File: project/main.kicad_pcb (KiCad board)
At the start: 6 copper layers, 160 x 257 mm, 207 parts

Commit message: adding comunication cable numbers
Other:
- board text added: "101"
- board text added: "102"
- board text added: "103"
- board text added: "106"
- board text added: "107"
- board text added: "108"
- board text added: "111"
- board text added: "112"
- board text added: "117"
- board text added: "118"
- board text added: "119"
- board text added: "120"
- board text added: "121"
- board text added: "122"
- board text added: "123"
- board text added: "217"
- board text added: "218"
- board text added: "219"
- board text added: "220"
- board text added: "221"
- board text added: "222"
- board text added: "223"
- board text added: "224"
- board text added: "317"
- board text added: "318"
- board text added: "3xx"
- board text added: "EL music 18m"
- board text added: "cam-dirty1 21m"
- board text added: "cam-dirty2 34m"
- board text added: "cam-laser 34m"
- board text added: "cam-storage1 16m"
- board text removed: "000"
- board text removed: "EL audio 18m"
- board text removed: "cam-purvinos1 21m"
- board text removed: "cam-purvinos2 34m"
- board text removed: "cam-sandelis1 16m"
- board text removed: "cam-staklide1 34m"
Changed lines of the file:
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@@
       (layer "F.SilkS" (type "Top Silk Screen") (color "Black"))
       (layer "F.Paste" (type "Top Solder Paste"))
-      (layer "F.Mask" (type "Top Solder Mask") (color "White") (thickness 0.01))
+      (layer "F.Mask" (type "Top Solder Mask") (thickness 0.01))
       (layer "F.Cu" (type "copper") (thickness 0.035))
-      (layer "dielectric 1" (type "core") (thickness 0.274) (material "FR4") (epsilon_r 4.5) (loss_tangent 0.02))
+      (layer "dielectric 1" (type "prepreg") (thickness 0.274) (material "FR4") (epsilon_r 4.5) (loss_tangent 0.02))
       (layer "In1.Cu" (type "copper") (thickness 0.035))
       (layer "dielectric 2" (type "prepreg") (thickness 0.274) (material "FR4") (epsilon_r 4.5) (loss_tangent 0.02))
@@
     (effects (font (size 2 2) (thickness 0.3)) (justify left))
   )
-  (gr_text "000" (at 170.28 50.32) (layer "User.5")
+  (gr_text "123" (at 170.28 50.32) (layer "User.5")
     (effects (font (size 1 1) (thickness 0.15)))
   )
@@
     (effects (font (size 1 1) (thickness 0.15)) (justify left))
   )
-  (gr_text "cam-sandelis1 16m" (at 42.28 145.32) (layer "User.5")
+  (gr_text "cam-storage1 16m" (at 42.28 145.32) (layer "User.5")
     (effects (font (size 2 2) (thickness 0.3)) (justify left))
   )
@@
     (effects (font (size 2 2) (thickness 0.3)) (justify left))
   )
-  (gr_text "000" (at 177.28 184.32) (layer "User.5")
+  (gr_text "106" (at 177.28 184.32) (layer "User.5")
     (effects (font (size 1 1) (thickness 0.15)))
   )
@@
     (effects (font (size 2 2) (thickness 0.3)) (justify left))
   )
-  (gr_text "000" (at 159.28 111.32) (layer "User.5")
+  (gr_text "102" (at 159.28 111.32) (layer "User.5")
     (effects (font (size 1 1) (thickness 0.15)))
   )
-  (gr_text "000" (at 129.28 207.32) (layer "User.5")
+  (gr_text "219" (at 129.28 207.32) (layer "User.5")
     (effects (font (size 1 1) (thickness 0.15)))
   )
@@
     (effects (font (size 1 1) (thickness 0.15)) (justify left))
   )
-  (gr_text "cam-staklide1\n34m" (at 174.28 47.32) (layer "User.5")
+  (gr_text "cam-laser\n34m" (at 174.28 47.32) (layer "User.5")
     (effects (font (size 2 2) (thickness 0.3)) (justify left))
   )
-  (gr_text "000" (at 196.28 65.32) (layer "User.5")
+  (gr_text "122" (at 196.28 65.32) (layer "User.5")
     (effects (font (size 1 1) (thickness 0.15)))
   )
@@
     (effects (font (size 2 2) (thickness 0.3)) (justify left))
   )
-  (gr_text "cam-purvinos1 21m" (at 43.28 111.32) (layer "User.5")
+  (gr_text "cam-dirty1 21m" (at 48.78 111.32) (layer "User.5")
     (effects (font (size 2 2) (thickness 0.3)) (justify left))
   )
@@
     (effects (font (size 1 1) (thickness 0.15)) (justify left))
   )
-  (gr_text "000" (at 115.28 86.32) (layer "User.5")
+  (gr_text "107" (at 115.28 86.32) (layer "User.5")
     (effects (font (size 1 1) (thickness 0.15)))
   )
-  (gr_text "000" (at 196.28 228.32) (layer "User.5")
+  (gr_text "118" (at 196.28 228.32) (layer "User.5")
     (effects (font (size 1 1) (thickness 0.15)))
   )
@@
     (effects (font (size 1 1) (thickness 0.15)) (justify left))
   )
-  (gr_text "000" (at 159.28 63.32) (layer "User.5")
+  (gr_text "111" (at 159.28 63.32) (layer "User.5")
     (effects (font (size 1 1) (thickness 0.15)))
   )
-  (gr_text "000" (at 174.28 231.32) (layer "User.5")
+  (gr_text "318" (at 174.28 231.32) (layer "User.5")
     (effects (font (size 1 1) (thickness 0.15)))
   )
@@
     (effects (font (size 1 1) (thickness 0.15)) (justify left))
   )
-  (gr_text "000" (at 155.28 268.32) (layer "User.5")
+  (gr_text "119" (at 155.28 268.32) (layer "User.5")
     (effects (font (size 1 1) (thickness 0.15)))
   )
@@
     (effects (font (size 2 2) (thickness 0.3)) (justify left))
   )
-  (gr_text "cam-el1 11m" (at 209.28 228.32) (layer "User.5")
+  (gr_text "cam-el2 11m" (at 209.28 228.32) (layer "User.5")
     (effects (font (size 2 2) (thickness 0.3)) (justify left))
   )
-  (gr_text "000" (at 86.28 111.32) (layer "User.5")
+  (gr_text "121" (at 86.28 111.32) (layer "User.5")
     (effects (font (size 1 1) (thickness 0.15)))
   )
@@
     (effects (font (size 2 2) (thickness 0.3)) (justify left))
   )
-  (gr_text "000" (at 128.28 184.32) (layer "User.5")
+  (gr_text "117" (at 128.28 184.32) (layer "User.5")
     (effects (font (size 1 1) (thickness 0.15)))
   )
@@
     (effects (font (size 1 1) (thickness 0.15)) (justify left))
   )
-  (gr_text "000" (at 115.28 42.32) (layer "User.5")
+  (gr_text "101" (at 115.28 42.32) (layer "User.5")
     (effects (font (size 1 1) (thickness 0.15)))
   )
@@
     (effects (font (size 1 1) (thickness 0.15)) (justify left))
   )
-  (gr_text "cam-purvinos2 34m" (at 208.28 65.32) (layer "User.5")
+  (gr_text "cam-dirty2 34m" (at 208.28 65.32) (layer "User.5")
     (effects (font (size 2 2) (thickness 0.3)) (justify left))
   )
@@
     (effects (font (size 1 1) (thickness 0.15)) (justify left))
   )
-  (gr_text "000" (at 133.28 231.32) (layer "User.5")
+  (gr_text "217" (at 133.28 231.32) (layer "User.5")
     (effects (font (size 1 1) (thickness 0.15)))
   )
@@
     (effects (font (size 1 1) (thickness 0.15)) (justify left))
   )
-  (gr_text "000" (at 202.28 184.32) (layer "User.5")
+  (gr_text "221" (at 202.28 184.32) (layer "User.5")
     (effects (font (size 1 1) (thickness 0.15)))
   )
@@
     (effects (font (size 2 2) (thickness 0.3)) (justify left))
   )
-  (gr_text "EL\naudio\n18m" (at 129.28 218.32) (layer "User.5")
+  (gr_text "EL\nmusic\n18m" (at 129.28 218.32) (layer "User.5")
     (effects (font (size 2 2) (thickness 0.3)) (justify left))
   )
@@
     (effects (font (size 2 2) (thickness 0.3)) (justify left))
   )
-  (gr_text "000" (at 170.28 39.32) (layer "User.5")
+  (gr_text "224" (at 170.28 39.32) (layer "User.5")
     (effects (font (size 1 1) (thickness 0.15)))
   )
@@
     (effects (font (size 2 2) (thickness 0.3)) (justify left))
   )
-  (gr_text "000" (at 133.28 184.32) (layer "User.5")
+  (gr_text "112" (at 133.28 184.32) (layer "User.5")
     (effects (font (size 1 1) (thickness 0.15)))
   )
-  (gr_text "000" (at 99.28 214.82) (layer "User.5")
+  (gr_text "218" (at 99.28 214.82) (layer "User.5")
     (effects (font (size 1 1) (thickness 0.15)))
   )
@@
     (effects (font (size 1 1) (thickness 0.15)) (justify left))
   )
-  (gr_text "cam-el2\n11m" (at 112.28 189.32) (layer "User.5")
+  (gr_text "cam-el1\n11m" (at 112.28 189.32) (layer "User.5")
     (effects (font (size 2 2) (thickness 0.3)) (justify left))
   )
@@
     (effects (font (size 1 1) (thickness 0.15)) (justify left))
   )
-  (gr_text "000" (at 150.28 187.32) (layer "User.5")
+  (gr_text "3xx" (at 150.28 187.32) (layer "User.5")
     (effects (font (size 1 1) (thickness 0.15)))
   )
@@
     (effects (font (size 2 2) (thickness 0.3)) (justify left))
   )
-  (gr_text "000" (at 138.28 231.32) (layer "User.5")
+  (gr_text "220" (at 138.28 231.32) (layer "User.5")
     (effects (font (size 1 1) (thickness 0.15)))
   )
@@
     (effects (font (size 1 1) (thickness 0.15)) (justify left))
   )
-  (gr_text "000" (at 86.28 164.32) (layer "User.5")
+  (gr_text "103" (at 86.28 164.32) (layer "User.5")
     (effects (font (size 1 1) (thickness 0.15)))
   )
@@
     (effects (font (size 1 1) (thickness 0.15)) (justify left))
   )
-  (gr_text "000" (at 159.28 231.32) (layer "User.5")
+  (gr_text "108" (at 159.28 231.32) (layer "User.5")
     (effects (font (size 1 1) (thickness 0.15)))
   )
@@
     (effects (font (size 1 1) (thickness 0.15)) (justify left))
   )
-  (gr_text "000" (at 202.28 187.32) (layer "User.5")
+  (gr_text "222" (at 202.28 187.32) (layer "User.5")
     (effects (font (size 1 1) (thickness 0.15)))
   )
-  (gr_text "000" (at 174.28 210.32) (layer "User.5")
+  (gr_text "317" (at 174.28 210.32) (layer "User.5")
     (effects (font (size 1 1) (thickness 0.15)))
   )
-  (gr_text "000" (at 170.28 36.32) (layer "User.5")
+  (gr_text "223" (at 170.28 36.32) (layer "User.5")
     (effects (font (size 1 1) (thickness 0.15)))
   )
-  (gr_text "000" (at 86.28 145.32) (layer "User.5")
+  (gr_text "120" (at 86.28 145.32) (layer "User.5")
     (effects (font (size 1 1) (thickness 0.15)))
   )

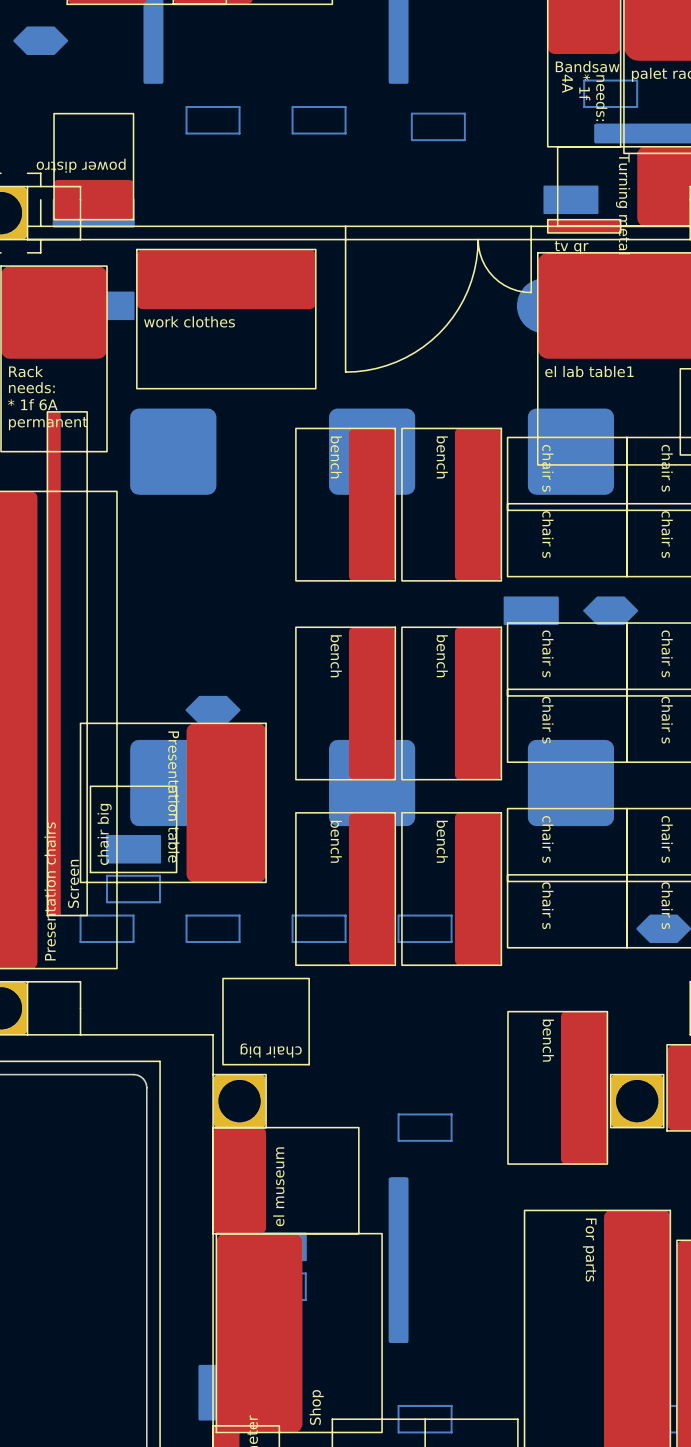
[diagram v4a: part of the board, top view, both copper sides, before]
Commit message: adding eth cables for power distribution boxes and tv2
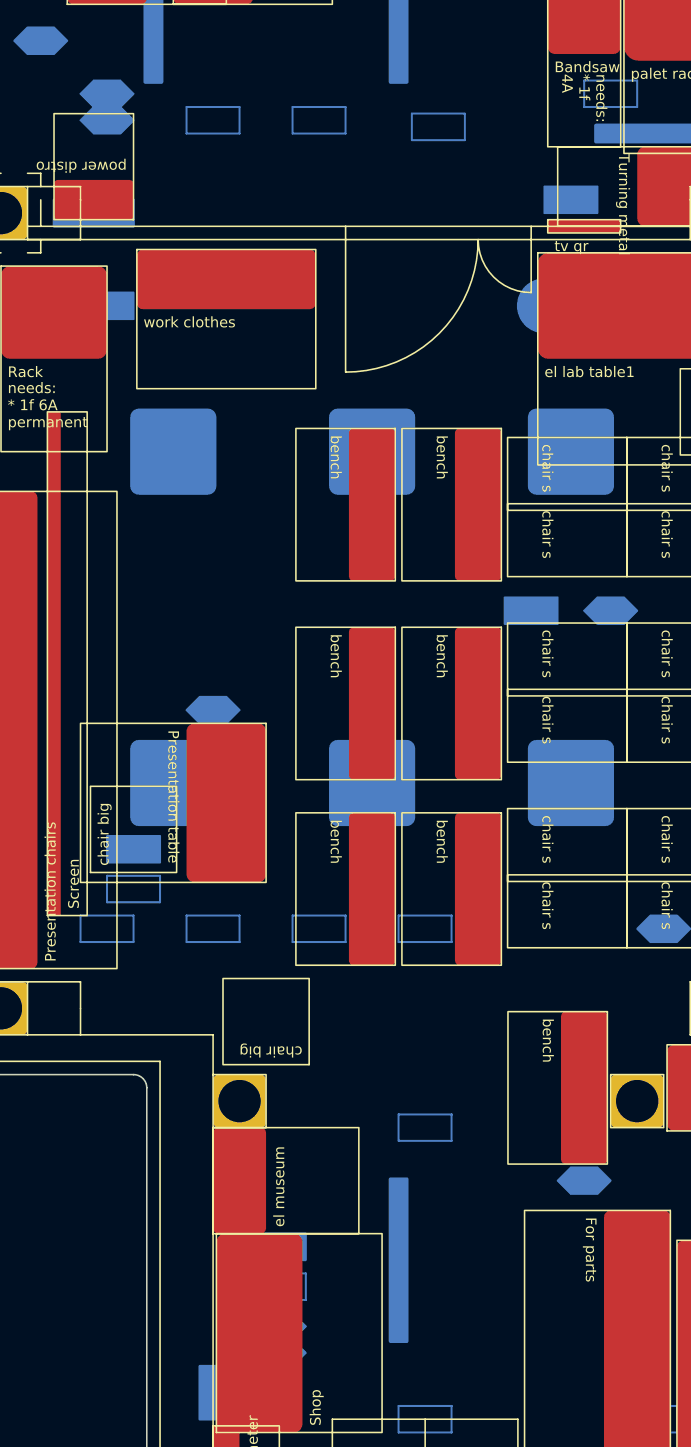
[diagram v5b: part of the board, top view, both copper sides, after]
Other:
- board text added: "???"
- board text added: "PDU-A-1 and PDU-A-2 - 2x22m"
- board text added: "PDU-B-1 and PDU-B-2 - 2x15m"
- board text added: "TV2 21m"
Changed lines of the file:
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@@
   (gr_rect (start 172.28 206.32) (end 176.28 208.32) (layer "B.Cu") (width 0.15) (fill solid))
   (gr_rect (start 186.28 264.32) (end 190.28 266.32) (layer "B.Cu") (width 0.15) (fill solid))
+  (gr_poly
+    (pts
+      (xy 129.28 250.32)
+      (xy 128.28 251.32)
+      (xy 126.28 251.32)
+      (xy 125.28 250.32)
+      (xy 126.28 249.32)
+      (xy 128.28 249.32)
+    ) (layer "B.Cu") (width 0.15) (fill solid))
   (gr_rect (start 144.28 234.32) (end 148.28 236.32) (layer "B.Cu") (width 0.15) (fill solid))
   (gr_poly
@@
   (gr_rect (start 84.28 62.32) (end 88.28 64.32) (layer "B.Cu") (width 0.15) (fill solid))
   (gr_rect (start 89.28 183.32) (end 93.28 185.32) (layer "B.Cu") (width 0.15) (fill solid))
+  (gr_poly
+    (pts
+      (xy 93.28 170.32)
+      (xy 92.28 171.32)
+      (xy 90.28 171.32)
+      (xy 89.28 170.32)
+      (xy 90.28 169.32)
+      (xy 92.28 169.32)
+    ) (layer "B.Cu") (width 0.15) (fill solid))
   (gr_rect (start 84.28 85.32) (end 88.28 87.32) (layer "B.Cu") (width 0.15) (fill solid))
   (gr_rect (start 239.28 109.32) (end 243.28 107.32) (layer "B.Cu") (width 0.15) (fill none))
@@
       (xy 241.28 111.32)
     ) (layer "B.Cu") (width 0.15) (fill solid))
+  (gr_poly
+    (pts
+      (xy 106.28 263.32)
+      (xy 105.28 264.32)
+      (xy 103.28 264.32)
+      (xy 102.28 263.32)
+      (xy 103.28 262.32)
+      (xy 105.28 262.32)
+    ) (layer "B.Cu") (width 0.15) (fill solid))
   (gr_rect (start 201.28 84.32) (end 205.28 82.32) (layer "B.Cu") (width 0.15) (fill none))
   (gr_poly
@@
   (gr_rect (start 186.28 261.32) (end 190.28 263.32) (layer "B.Cu") (width 0.15) (fill solid))
   (gr_rect (start 84.28 124.32) (end 88.28 122.32) (layer "B.Cu") (width 0.15) (fill none))
+  (gr_poly
+    (pts
+      (xy 93.28 168.32)
+      (xy 92.28 169.32)
+      (xy 90.28 169.32)
+      (xy 89.28 168.32)
+      (xy 90.28 167.32)
+      (xy 92.28 167.32)
+    ) (layer "B.Cu") (width 0.15) (fill solid))
   (gr_rect (start 142.28 232.32) (end 146.28 230.32) (layer "B.Cu") (width 0.15) (fill none))
   (gr_rect (start 97.28 232.32) (end 101.28 230.32) (layer "B.Cu") (width 0.15) (fill none))
@@
   (gr_rect (start 105.28 112.32) (end 109.28 110.32) (layer "B.Cu") (width 0.15) (fill none))
   (gr_rect (start 157.28 185.32) (end 161.28 183.32) (layer "B.Cu") (width 0.15) (fill none))
+  (gr_poly
+    (pts
+      (xy 106.28 261.32)
+      (xy 105.28 262.32)
+      (xy 103.28 262.32)
+      (xy 102.28 261.32)
+      (xy 103.28 260.32)
+      (xy 105.28 260.32)
+    ) (layer "B.Cu") (width 0.15) (fill solid))
   (gr_poly
     (pts
@@
   (gr_line (start 115.28 83.32) (end 114.28 84.32) (layer "User.5") (width 0.15))
   (gr_line (start 128.28 188.32) (end 127.28 189.32) (layer "User.5") (width 0.15))
+  (gr_line (start 87.28 168.32) (end 88.28 169.32) (layer "User.5") (width 0.15))
   (gr_line (start 128.28 210.32) (end 129.28 209.32) (layer "User.5") (width 0.15))
   (gr_line (start 160.28 66.32) (end 158.28 66.32) (layer "User.5") (width 0.15))
@@
   (gr_line (start 132.28 186.32) (end 133.28 187.32) (layer "User.5") (width 0.15))
   (gr_line (start 78.28 187.32) (end 78.28 186.32) (layer "User.5") (width 0.15))
+  (gr_line (start 97.28 261.32) (end 97.28 260.32) (layer "User.5") (width 0.15))
   (gr_line (start 153.28 265.32) (end 155.28 265.32) (layer "User.5") (width 0.15))
   (gr_line (start 203.28 227.32) (end 203.28 229.32) (layer "User.5") (width 0.15))
@@
   (gr_line (start 98.28 212.32) (end 100.28 212.32) (layer "User.5") (width 0.15))
   (gr_line (start 203.28 66.32) (end 202.28 65.32) (layer "User.5") (width 0.15))
+  (gr_line (start 97.28 260.32) (end 98.28 261.32) (layer "User.5") (width 0.15))
   (gr_line (start 119.28 42.32) (end 121.28 42.32) (layer "User.5") (width 0.15))
   (gr_line (start 207.28 187.32) (end 208.28 186.32) (layer "User.5") (width 0.15))
   (gr_line (start 174.28 235.32) (end 174.28 237.32) (layer "User.5") (width 0.15))
+  (gr_line (start 88.28 169.32) (end 87.28 170.32) (layer "User.5") (width 0.15))
+  (gr_line (start 128.28 253.32) (end 127.28 252.32) (layer "User.5") (width 0.15))
   (gr_line (start 207.28 184.32) (end 208.28 183.32) (layer "User.5") (width 0.15))
   (gr_line (start 203.28 229.32) (end 202.28 228.32) (layer "User.5") (width 0.15))
@@
   (gr_line (start 174.28 49.32) (end 174.28 51.32) (layer "User.5") (width 0.15))
   (gr_line (start 175.28 235.32) (end 173.28 235.32) (layer "User.5") (width 0.15))
+  (gr_line (start 127.28 254.32) (end 127.28 253.32) (layer "User.5") (width 0.15))
+  (gr_line (start 126.28 253.32) (end 127.28 252.32) (layer "User.5") (width 0.15))
   (gr_line (start 118.28 42.32) (end 119.28 41.32) (layer "User.5") (width 0.15))
+  (gr_line (start 74.28 169.32) (end 87.28 169.32) (layer "User.5") (width 0.15))
   (gr_line (start 80.28 164.32) (end 79.28 165.32) (layer "User.5") (width 0.15))
+  (gr_line (start 87.28 169.32) (end 87.28 170.32) (layer "User.5") (width 0.15))
   (gr_line (start 149.28 190.82) (end 150.28 189.82) (layer "User.5") (width 0.15))
   (gr_line (start 173.28 36.32) (end 174.28 35.32) (layer "User.5") (width 0.15))
   (gr_line (start 138.28 228.32) (end 137.28 229.32) (layer "User.5") (width 0.15))
   (gr_line (start 174.28 37.32) (end 173.28 36.32) (layer "User.5") (width 0.15))
+  (gr_line (start 128.28 253.32) (end 126.28 253.32) (layer "User.5") (width 0.15))
   (gr_line (start 174.28 38.32) (end 174.28 40.32) (layer "User.5") (width 0.15))
   (gr_line (start 79.28 145.32) (end 73.28 145.32) (layer "User.5") (width 0.15))
   (gr_line (start 159.28 65.32) (end 160.28 66.32) (layer "User.5") (width 0.15))
+  (gr_line (start 98.28 261.32) (end 97.28 262.32) (layer "User.5") (width 0.15))
   (gr_line (start 114.28 83.32) (end 114.28 81.32) (layer "User.5") (width 0.15))
   (gr_line (start 174.28 50.32) (end 176.28 50.32) (layer "User.5") (width 0.15))
@@
   (gr_line (start 159.28 229.32) (end 161.28 229.32) (layer "User.5") (width 0.15))
   (gr_line (start 179.28 184.32) (end 180.28 183.32) (layer "User.5") (width 0.15))
+  (gr_line (start 87.28 169.32) (end 87.28 168.32) (layer "User.5") (width 0.15))
   (gr_line (start 173.28 50.32) (end 174.28 49.32) (layer "User.5") (width 0.15))
   (gr_line (start 150.28 190.82) (end 150.28 198.32) (layer "User.5") (width 0.15))
@@
   (gr_line (start 203.28 64.32) (end 203.28 66.32) (layer "User.5") (width 0.15))
   (gr_line (start 160.28 230.32) (end 159.28 229.32) (layer "User.5") (width 0.15))
+  (gr_line (start 92.28 261.32) (end 97.28 261.32) (layer "User.5") (width 0.15))
+  (gr_line (start 97.28 261.32) (end 97.28 262.32) (layer "User.5") (width 0.15))
   (gr_line (start 119.28 41.32) (end 119.28 43.32) (layer "User.5") (width 0.15))
   (gr_line (start 174.28 39.32) (end 176.28 39.32) (layer "User.5") (width 0.15))
@@
     (effects (font (size 2 2) (thickness 0.3)) (justify left))
   )
-  (gr_text "7x0.75\nB2 21m\nD551\n~D553" (at 115.28 260.32) (layer "User.3")
+  (gr_text "7x0.75\nB2 21m\nD551\n~D553" (at 116.28 261.32) (layer "User.3")
     (effects (font (size 2 2) (thickness 0.3)) (justify left))
   )
@@
     (effects (font (size 1 1) (thickness 0.15)) (justify left))
   )
+  (gr_text "???" (at 104.28 261.32) (layer "User.5")
+    (effects (font (size 1 1) (thickness 0.15)))
+  )
   (gr_text "21" (at 136.28 111.32) (layer "User.5")
     (effects (font (size 1 1) (thickness 0.15)) (justify left))
@@
     (effects (font (size 2 2) (thickness 0.3)) (justify left))
   )
+  (gr_text "???" (at 127.28 250.32) (layer "User.5")
+    (effects (font (size 1 1) (thickness 0.15)))
+  )
   (gr_text "106" (at 177.28 184.32) (layer "User.5")
     (effects (font (size 1 1) (thickness 0.15)))
@@
     (effects (font (size 1 1) (thickness 0.15)) (justify left))
   )
+  (gr_text "PDU-B-1 and PDU-B-2 - 2x15m" (at 74.28 169.32) (layer "User.5")
+    (effects (font (size 2 2) (thickness 0.3)) (justify right))
+  )
   (gr_text "221" (at 202.28 184.32) (layer "User.5")
     (effects (font (size 1 1) (thickness 0.15)))
@@
   (gr_text "xxx" (at 241.28 128.32) (layer "User.5")
     (effects (font (size 1 1) (thickness 0.15)))
+  )
+  (gr_text "???" (at 91.28 170.32) (layer "User.5")
+    (effects (font (size 1 1) (thickness 0.15)))
+  )
+  (gr_text "PDU-A-1 and PDU-A-2 - 2x22m" (at 92.28 261.32) (layer "User.5")
+    (effects (font (size 2 2) (thickness 0.3)) (justify right))
   )
   (gr_text "18" (at 108.28 268.32) (layer "User.5")
@@
     (effects (font (size 1 1) (thickness 0.15)) (justify left))
   )
+  (gr_text "TV2\n21m" (at 119.28 252.32) (layer "User.5")
+    (effects (font (size 2 2) (thickness 0.3)) (justify left))
+  )
   (gr_text "3xx" (at 150.28 187.32) (layer "User.5")
     (effects (font (size 1 1) (thickness 0.15)))
@@
     (effects (font (size 1 1) (thickness 0.15)) (justify left))
   )
+  (gr_text "???" (at 91.28 168.32) (layer "User.5")
+    (effects (font (size 1 1) (thickness 0.15)))
+  )
   (gr_text "103" (at 86.28 164.32) (layer "User.5")
     (effects (font (size 1 1) (thickness 0.15)))
@@
     (effects (font (size 1 1) (thickness 0.15)))
   )
+  (gr_text "???" (at 104.28 263.32) (layer "User.5")
+    (effects (font (size 1 1) (thickness 0.15)))
+  )
